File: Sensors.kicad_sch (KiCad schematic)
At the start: 12 parts, among them U3 MMC5983MA, U4 ICM-42688-P, U7 MS5607-02BA, U8 ADXL375

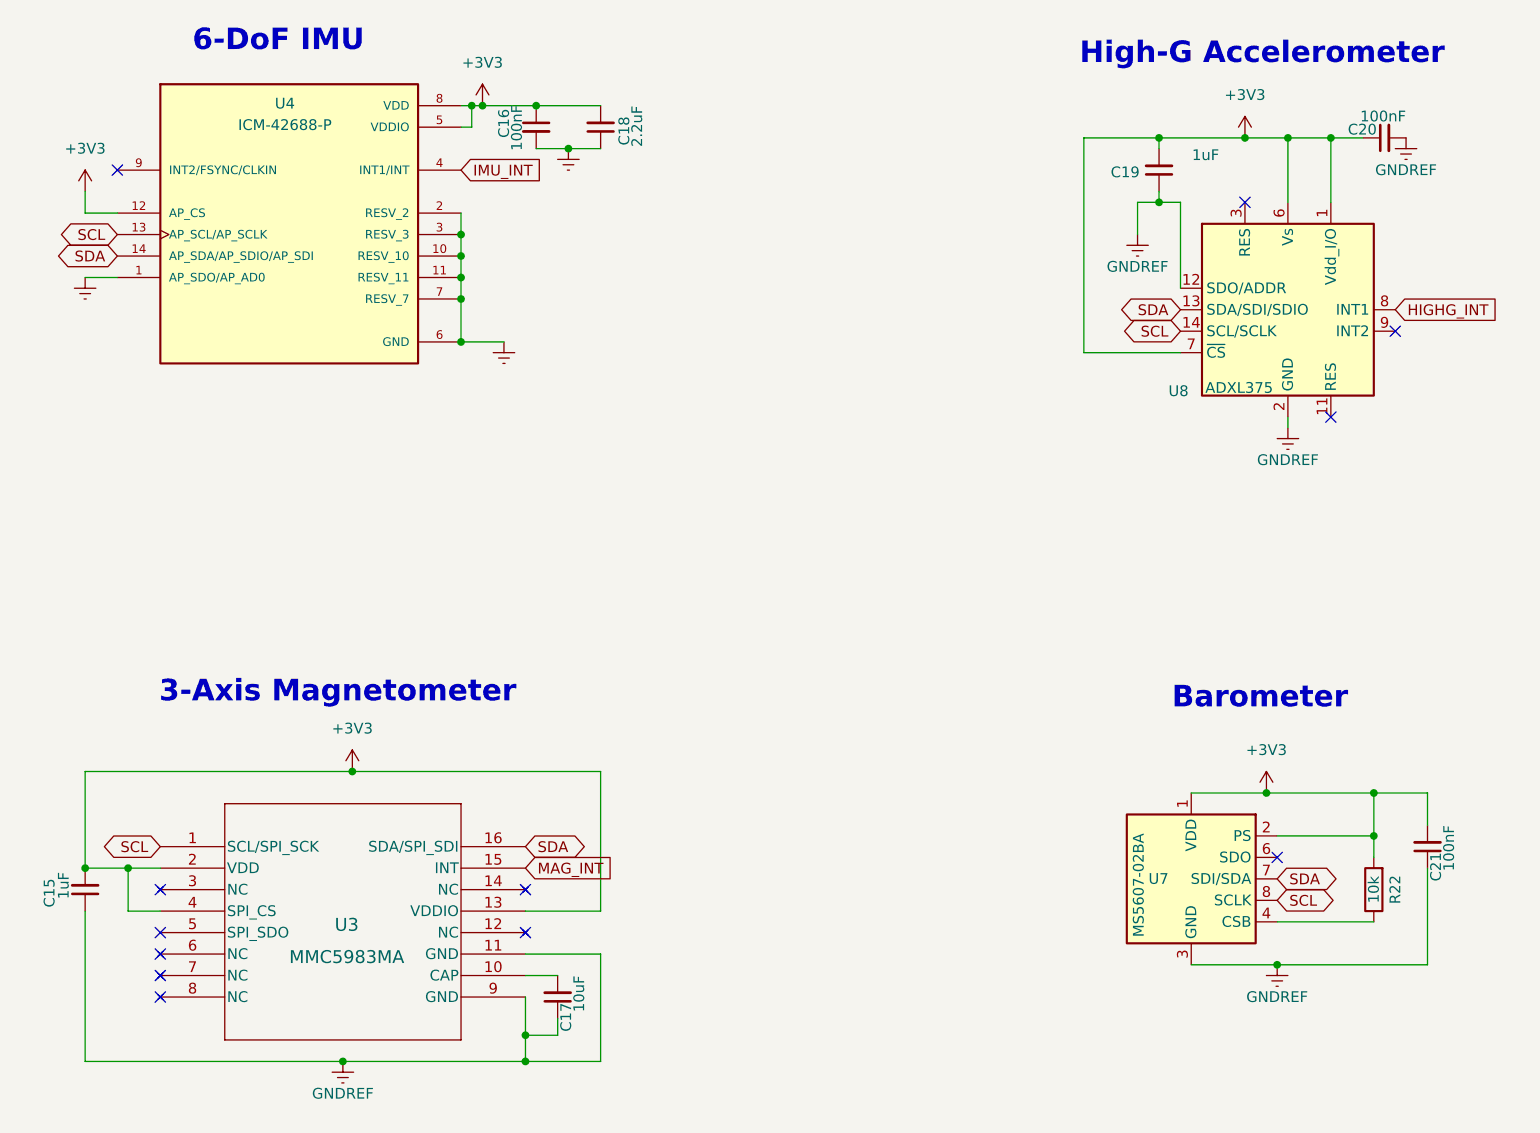
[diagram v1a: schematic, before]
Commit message: updated power delivery and component choices. v4 now ready
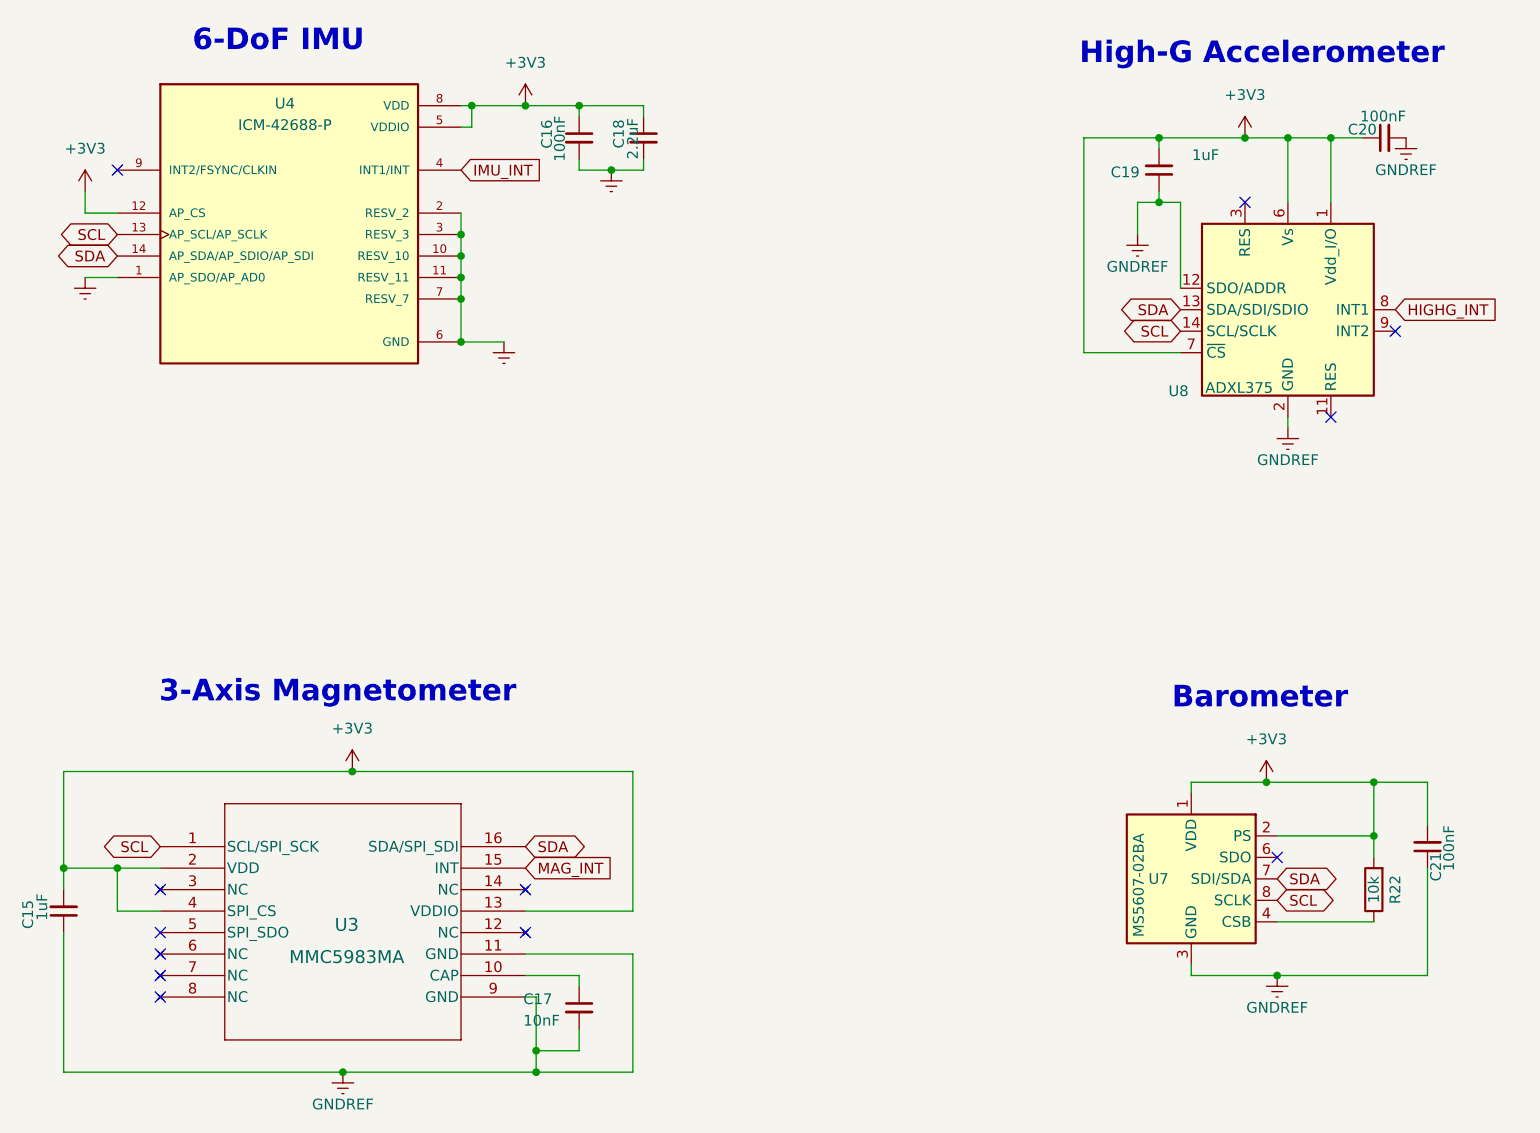
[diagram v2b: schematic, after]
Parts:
- C17: value 10uF -> 10nF; LCSC C15525 -> (none)
- C18: footprint Capacitor_SMD:C_0402_1005Metric -> Capacitor_SMD:C_0603_1608Metric; LCSC C12530 -> C23630; Product ID GRM155C71A225KE11J -> GRM188C71C225ME11D
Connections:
- net +3V3: now also C18.1; no longer C18.2
- net GNDREF: now also C17.2, C18.2; no longer C17.1, C18.1
- net at U3.10 (CAP): now also C17.1; no longer C17.2
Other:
- moved on the sheet: C15, C16

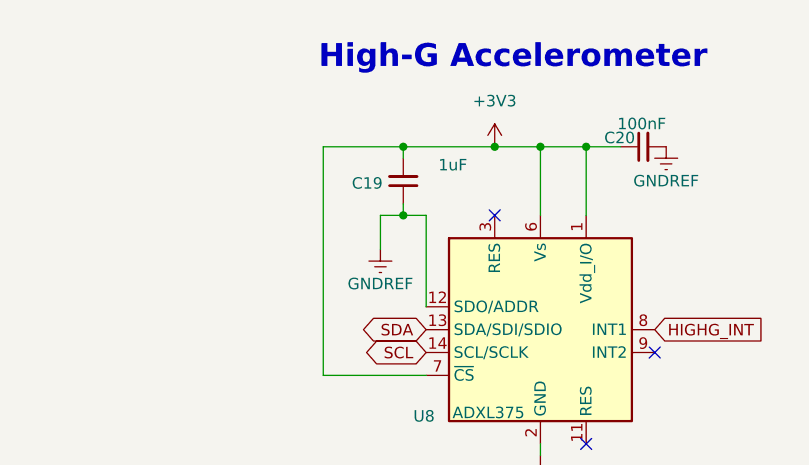
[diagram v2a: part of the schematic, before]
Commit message: Fixed power distribution and made small improvements. Updated revision number
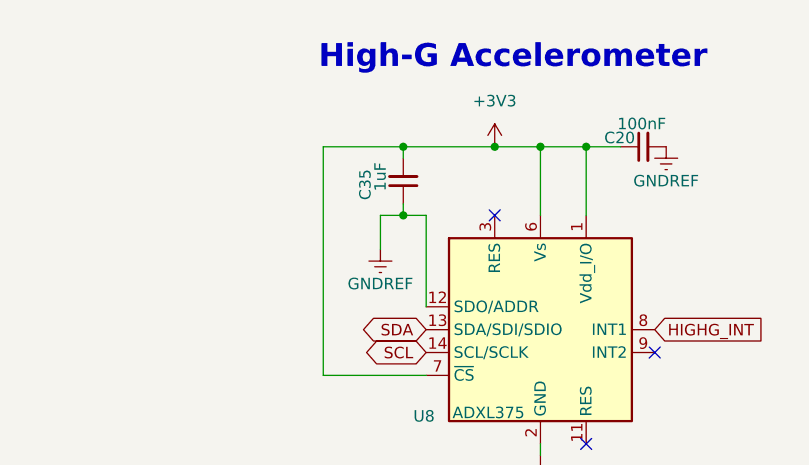
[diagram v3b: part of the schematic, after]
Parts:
- removed C19: 1uF, Capacitor_SMD:C_0402_1005Metric, symbol Device:C_Small
- added C35: 1uF, Capacitor_SMD:C_0603_1608Metric, symbol Device:C_Small
- C15: footprint Capacitor_SMD:C_0402_1005Metric -> Capacitor_SMD:C_0603_1608Metric; LCSC C52923 -> (none); Product ID GRT153R61A105ME13D -> CL10B105KP8NNNC
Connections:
- net +3V3: now also C35.2
- net GNDREF: now also C35.1
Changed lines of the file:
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@@
 	(title_block
 		(title "WINTER Sensors")
-		(date "2025-08-28")
-		(rev "4-Dev")
+		(date "2025-11-24")
+		(rev "4.1")
 		(company "SparrowTheNerd")
 	)
@@
 			)
 		)
-		(property "Footprint" "Capacitor_SMD:C_0402_1005Metric"
+		(property "Footprint" "Capacitor_SMD:C_0603_1608Metric"
 			(at 63.5 133.35 0)
 			(effects
@@
 			)
 		)
-		(property "Product ID" "GRT153R61A105ME13D"
+		(property "Product ID" "CL10B105KP8NNNC "
 			(at 63.5 133.35 0)
 			(effects
@@
 			)
 		)
-		(property "LCSC" "C52923"
+		(property "LCSC" ""
 			(at 63.5 133.35 0)
 			(effects
@@
 				(path "/b8dcf6c3-e00e-4510-86f1-1869a84939df/595bc435-8840-4b57-9d45-84e2c6628ca1"
 					(reference "C20")
+					(unit 1)
+				)
+			)
+		)
+	)
+	(symbol
+		(lib_id "Device:C_Small")
+		(at 193.04 45.72 180)
+		(unit 1)
+		(exclude_from_sim no)
+		(in_bom yes)
+		(on_board yes)
+		(dnp no)
+		(property "Reference" "C35"
+			(at 188.8236 44.3992 90)
+			(effects
+				(font
+					(size 1.27 1.27)
+				)
+				(justify left)
+			)
+		)
+		(property "Value" "1uF"
+			(at 190.5 43.6372 90)
+			(effects
+				(font
+					(size 1.27 1.27)
+				)
+				(justify left)
+			)
+		)
+		(property "Footprint" "Capacitor_SMD:C_0603_1608Metric"
+			(at 193.04 45.72 0)
+			(effects
+				(font
+					(size 1.27 1.27)
+				)
+				(hide yes)
+			)
+		)
+		(property "Datasheet" "~"
+			(at 193.04 45.72 0)
+			(effects
+				(font
+					(size 1.27 1.27)
+				)
+				(hide yes)
+			)
+		)
+		(property "Description" "Unpolarized capacitor, small symbol"
+			(at 193.04 45.72 0)
+			(effects
+				(font
+					(size 1.27 1.27)
+				)
+				(hide yes)
+			)
+		)
+		(property "Price" ""
+			(at 193.04 45.72 0)
+			(effects
+				(font
+					(size 1.27 1.27)
+				)
+				(hide yes)
+			)
+		)
+		(property "Price Per Item" ""
+			(at 193.04 45.72 0)
+			(effects
+				(font
+					(size 1.27 1.27)
+				)
+				(hide yes)
+			)
+		)
+		(property "Product ID" "CL10B105KP8NNNC "
+			(at 193.04 45.72 0)
+			(effects
+				(font
+					(size 1.27 1.27)
+				)
+				(hide yes)
+			)
+		)
+		(property "LCSC" ""
+			(at 193.04 45.72 0)
+			(effects
+				(font
+					(size 1.27 1.27)
+				)
+				(hide yes)
+			)
+		)
+		(property "Mouser ID" ""
+			(at 193.04 45.72 0)
+			(effects
+				(font
+					(size 1.27 1.27)
+				)
+				(hide yes)
+			)
+		)
+		(pin "1"
+		)
+		(pin "2"
+		)
+		(instances
+			(project "WINTER"
+				(path "/b8dcf6c3-e00e-4510-86f1-1869a84939df/595bc435-8840-4b57-9d45-84e2c6628ca1"
+					(reference "C35")
 					(unit 1)
 				)
@@
 	)
 	(symbol
-		(lib_id "Device:C_Small")
-		(at 124.46 144.78 0)
-		(unit 1)
-		(exclude_from_sim no)
-		(in_bom yes)
-		(on_board yes)
-		(dnp no)
-		(property "Reference" "C17"
-			(at 117.856 143.764 0)
-			(effects
-				(font
-					(size 1.27 1.27)
-				)
-				(justify left)
-			)
-		)
-		(property "Value" "10nF"
-			(at 117.856 146.304 0)
-			(effects
-				(font
-					(size 1.27 1.27)
-				)
-				(justify left)
-			)
-		)
-		(property "Footprint" "Capacitor_SMD:C_0603_1608Metric"
-			(at 124.46 144.78 0)
-			(effects
-				(font
-					(size 1.27 1.27)
-				)
-				(hide yes)
-			)
-		)
-		(property "Datasheet" "~"
-			(at 124.46 144.78 0)
-			(effects
-				(font
-					(size 1.27 1.27)
-				)
-				(hide yes)
-			)
-		)
-		(property "Description" "Unpolarized capacitor, small symbol"
-			(at 124.46 144.78 0)
-			(effects
-				(font
-					(size 1.27 1.27)
-				)
-				(hide yes)
-			)
-		)
-		(property "Product ID" "GRM155R61A106ME11D"
-			(at 124.46 144.78 0)
-			(effects
-				(font
-					(size 1.27 1.27)
-				)
-				(hide yes)
-			)
-		)
-		(pin "1"
-		)
-		(pin "2"
-		)
-		(instances
-			(project "WINTER"
-				(path "/b8dcf6c3-e00e-4510-86f1-1869a84939df/595bc435-8840-4b57-9d45-84e2c6628ca1"
-					(reference "C17")
-					(unit 1)
-				)
-			)
-		)
-	)
-	(symbol
 		(lib_id "Device:R")
 		(at 218.44 130.81 180)
@@
 	(symbol
 		(lib_id "Device:C_Small")
-		(at 193.04 45.72 180)
+		(at 124.46 144.78 0)
 		(unit 1)
 		(exclude_from_sim no)
@@
 		(on_board yes)
 		(dnp no)
-		(property "Reference" "C19"
-			(at 190.754 45.974 0)
+		(property "Reference" "C17"
+			(at 117.856 143.764 0)
 			(effects
 				(font
@@
 			)
 		)
-		(property "Value" "1uF"
-			(at 200.152 43.942 0)
+		(property "Value" "10nF"
+			(at 117.856 146.304 0)
 			(effects
 				(font
@@
 			)
 		)
-		(property "Footprint" "Capacitor_SMD:C_0402_1005Metric"
-			(at 193.04 45.72 0)
+		(property "Footprint" "Capacitor_SMD:C_0603_1608Metric"
+			(at 124.46 144.78 0)
 			(effects
 				(font
@@
 		)
 		(property "Datasheet" "~"
-			(at 193.04 45.72 0)
+			(at 124.46 144.78 0)
 			(effects
 				(font
@@
 		)
 		(property "Description" "Unpolarized capacitor, small symbol"
-			(at 193.04 45.72 0)
-			(effects
-				(font
-					(size 1.27 1.27)
-				)
-				(hide yes)
-			)
-		)
-		(property "Price" ""
-			(at 193.04 45.72 0)
-			(effects
-				(font
-					(size 1.27 1.27)
-				)
-				(hide yes)
-			)
-		)
-		(property "Price Per Item" ""
-			(at 193.04 45.72 0)
-			(effects
-				(font
-					(size 1.27 1.27)
-				)
-				(hide yes)
-			)
-		)
-		(property "Product ID" "GRT153R61A105ME13D"
-			(at 193.04 45.72 0)
-			(effects
-				(font
-					(size 1.27 1.27)
-				)
-				(hide yes)
-			)
-		)
-		(property "LCSC" "C52923"
-			(at 193.04 45.72 0)
-			(effects
-				(font
-					(size 1.27 1.27)
-				)
-				(hide yes)
-			)
-		)
-		(property "Mouser ID" ""
-			(at 193.04 45.72 0)
+			(at 124.46 144.78 0)
+			(effects
+				(font
+					(size 1.27 1.27)
+				)
+				(hide yes)
+			)
+		)
+		(property "Product ID" "GRM155R61A106ME11D"
+			(at 124.46 144.78 0)
 			(effects
 				(font
@@
 		)
 		(instances
-			(project "SAP Mk3.3"
+			(project "WINTER"
 				(path "/b8dcf6c3-e00e-4510-86f1-1869a84939df/595bc435-8840-4b57-9d45-84e2c6628ca1"
-					(reference "C19")
+					(reference "C17")
 					(unit 1)
 				)
